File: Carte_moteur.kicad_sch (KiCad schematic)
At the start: 24 parts, among them J101 Conn_01x02_Socket, J102 Conn_01x02, J103 Conn_01x02, J104 Conn_01x05_Pin, J105 Conn_01x05_Pin, J106 Conn_01x05_Pin, J107 Conn_01x07, U101 LD1117S33TR_SOT223

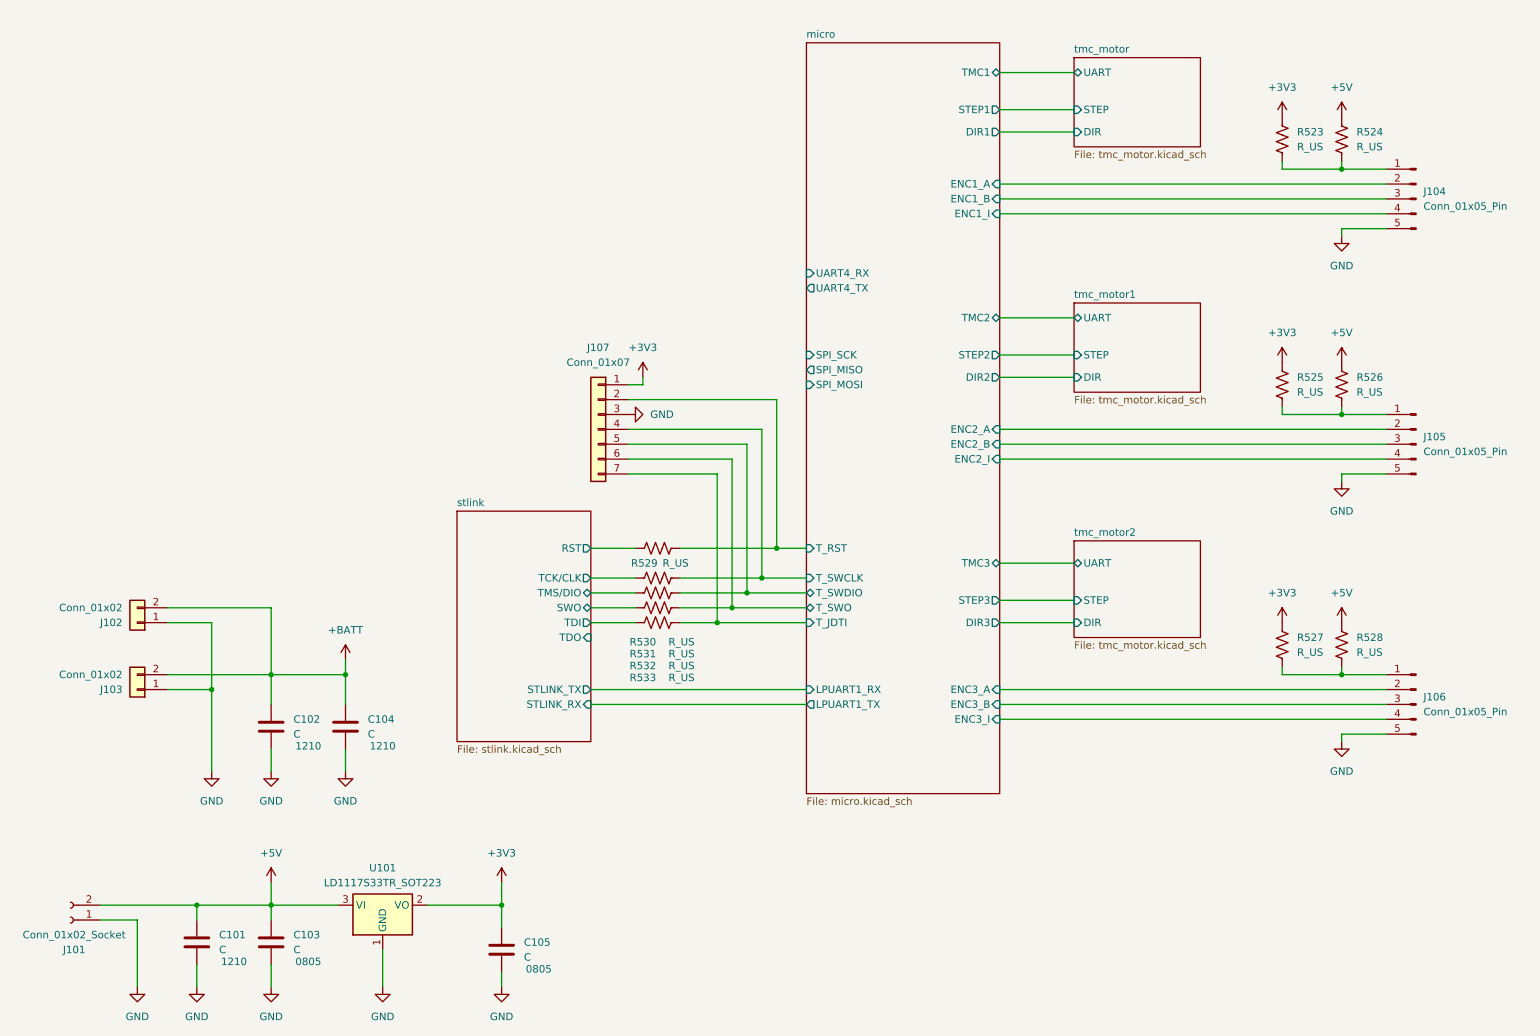
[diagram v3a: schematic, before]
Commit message: Add net class
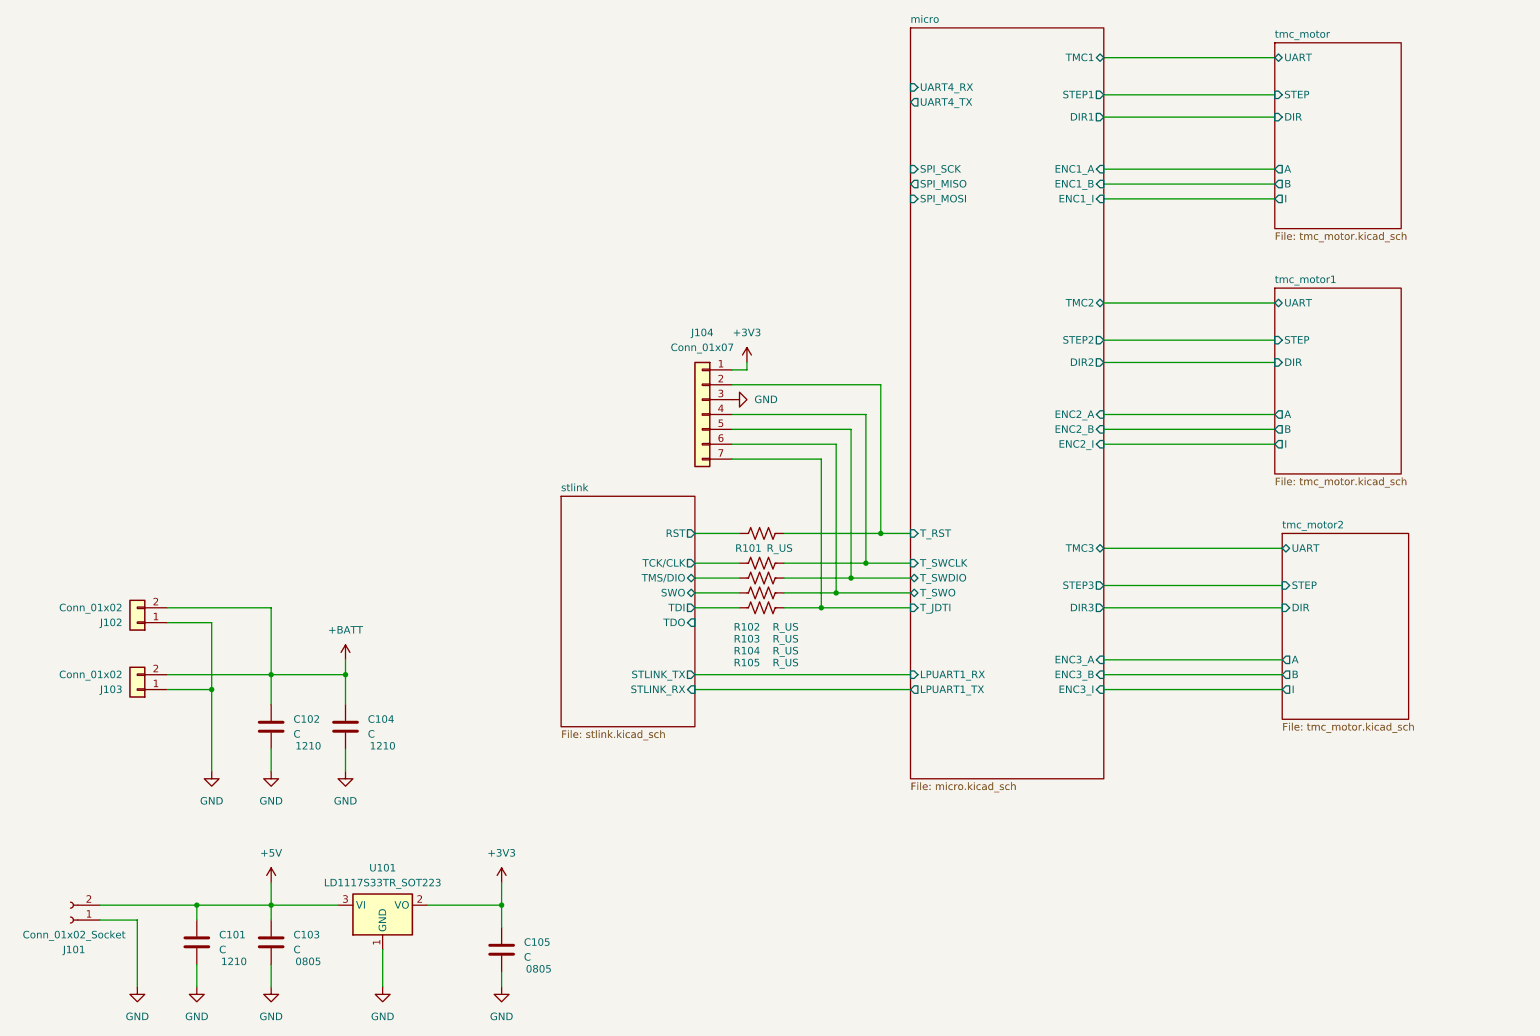
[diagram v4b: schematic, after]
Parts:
- removed J104, J105, J106: Conn_01x05_Pin, Connector_Molex:Molex_KK-254_AE-6410-05A_1x05_P2.54mm_Vertical, symbol Connector:Conn_01x05_Pin
- removed R523, R524, R525, R526, R527, R528: R_US, Resistor_SMD:R_0603_1608Metric_Pad0.98x0.95mm_HandSolder, symbol Device:R_US
- renumbered J107 to J104, R529 to R101, R530 to R102, R531 to R103, R532 to R104, R533 to R105
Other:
- sheet tmc_motor ports: added A, B, I; removed none
- sheet tmc_motor1 ports: added A, B, I; removed none
- sheet tmc_motor2 ports: added A, B, I; removed none
- moved on the sheet: J104, R101, R102, R103, R104, R105

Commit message: move encoder pull up resistor to tmc sheet
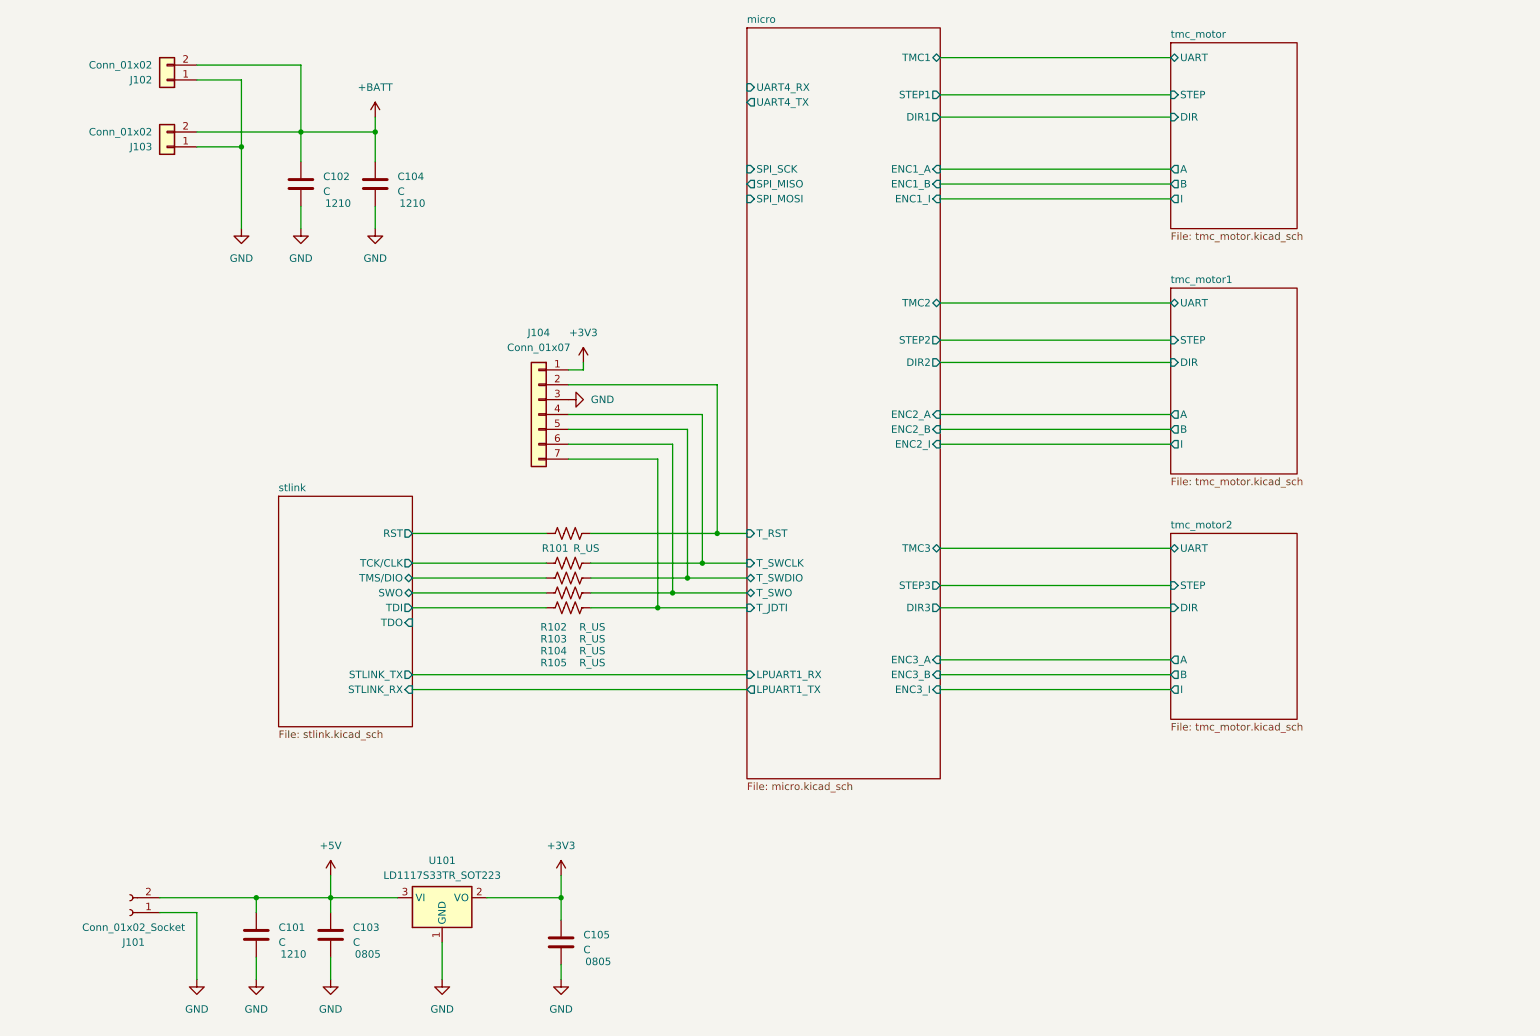
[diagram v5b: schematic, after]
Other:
- moved on the sheet: C101, C102, C103, C104, C105, J101, J102, J103, J104, R101, R102, R103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

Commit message: before trying new µC orientation
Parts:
- added J105: Conn_01x02_Socket, Connector_Molex:Molex_KK-396_A-41791-0002_1x02_P3.96mm_Vertical, symbol Connector:Conn_01x02_Socket
- added J106: Conn_01x07, Connector_Molex:Molex_KK-254_AE-6410-07A_1x07_P2.54mm_Vertical, symbol Connector_Generic:Conn_01x07
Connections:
- net +5V: now also J105.2 (Pin_2)
- net GND: now also J105.1 (Pin_1), J106.1 (Pin_1), J106.4 (Pin_4)
- net micro/SPI_MISO: now also J106.6 (Pin_6)
- net micro/SPI_MOSI: now also J106.7 (Pin_7)
- net micro/SPI_SCK: now also J106.5 (Pin_5)
- net micro/UART4_RX: now also J106.2 (Pin_2)
- net micro/UART4_TX: now also J106.3 (Pin_3)

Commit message: almost done
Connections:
- net micro/LPUART1_RX: now also J106.2 (Pin_2)
- net micro/LPUART1_TX: now also J106.3 (Pin_3)
- net micro/T_JDTI: now also J104.6 (Pin_6); no longer J104.7 (Pin_7)
- net micro/T_SWCLK: now also J104.5 (Pin_5); no longer J104.4 (Pin_4)
- net micro/T_SWDIO: now also J104.4 (Pin_4); no longer J104.5 (Pin_5)
- net micro/T_SWO: now also J104.7 (Pin_7); no longer J104.6 (Pin_6)
- net micro/UART4_RX: no longer J106.2 (Pin_2)
- net micro/UART4_TX: no longer J106.3 (Pin_3)
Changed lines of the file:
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@@
 	)
 	(junction
+		(at 124.46 118.11)
+		(diameter 0)
+		(color 0 0 0 0)
+	)
+	(junction
 		(at 45.72 172.72)
 		(diameter 0)
@@
 	)
 	(junction
-		(at 127 118.11)
+		(at 129.54 113.03)
 		(diameter 0)
 		(color 0 0 0 0)
 	)
 	(junction
-		(at 129.54 115.57)
+		(at 132.08 115.57)
 		(diameter 0)
 		(color 0 0 0 0)
 	)
 	(junction
-		(at 76.2 39.37)
+		(at 127 120.65)
 		(diameter 0)
 		(color 0 0 0 0)
 	)
 	(junction
-		(at 63.5 39.37)
+		(at 76.2 39.37)
 		(diameter 0)
 		(color 0 0 0 0)
 	)
 	(junction
-		(at 124.46 120.65)
+		(at 63.5 39.37)
 		(diameter 0)
 		(color 0 0 0 0)
@@
 		(color 0 0 0 0)
 	)
-	(junction
-		(at 132.08 113.03)
-		(diameter 0)
-		(color 0 0 0 0)
-	)
 	(wire
 		(pts
@@
 	(wire
 		(pts
-			(xy 129.54 90.17) (xy 129.54 115.57)
+			(xy 53.34 30.48) (xy 45.72 30.48)
 		)
 		(stroke
@@
 	(wire
 		(pts
-			(xy 53.34 30.48) (xy 45.72 30.48)
+			(xy 63.5 39.37) (xy 63.5 27.94)
 		)
 		(stroke
@@
 	(wire
 		(pts
-			(xy 63.5 39.37) (xy 63.5 27.94)
+			(xy 82.55 132.08) (xy 139.7 132.08)
 		)
 		(stroke
@@
 	(wire
 		(pts
-			(xy 113.03 113.03) (xy 132.08 113.03)
+			(xy 113.03 113.03) (xy 129.54 113.03)
+		)
+		(stroke
+			(width 0)
+			(type default)
+		)
+	)
+	(wire
+		(pts
+			(xy 124.46 118.11) (xy 139.7 118.11)
 		)
 		(stroke
@@
 	(wire
 		(pts
-			(xy 116.84 55.88) (xy 116.84 43.18)
+			(xy 109.22 38.1) (xy 139.7 38.1)
 		)
 		(stroke
@@
 	(wire
 		(pts
-			(xy 76.2 39.37) (xy 63.5 39.37)
+			(xy 116.84 55.88) (xy 116.84 43.18)
 		)
 		(stroke
@@
 	(wire
 		(pts
-			(xy 134.62 82.55) (xy 134.62 107.95)
+			(xy 127 92.71) (xy 127 120.65)
 		)
 		(stroke
@@
 	(wire
 		(pts
-			(xy 109.22 38.1) (xy 139.7 38.1)
+			(xy 76.2 39.37) (xy 63.5 39.37)
 		)
 		(stroke
@@
 	(wire
 		(pts
-			(xy 76.2 39.37) (xy 76.2 44.45)
+			(xy 134.62 82.55) (xy 134.62 107.95)
 		)
 		(stroke
@@
 	(wire
 		(pts
-			(xy 132.08 113.03) (xy 139.7 113.03)
+			(xy 76.2 39.37) (xy 76.2 44.45)
 		)
 		(stroke
@@
 	(wire
 		(pts
-			(xy 109.22 35.56) (xy 116.84 35.56)
+			(xy 132.08 115.57) (xy 139.7 115.57)
 		)
 		(stroke
@@
 	(wire
 		(pts
-			(xy 113.03 118.11) (xy 127 118.11)
+			(xy 109.22 35.56) (xy 116.84 35.56)
 		)
 		(stroke
@@
 	(wire
 		(pts
-			(xy 124.46 95.25) (xy 124.46 120.65)
-		)
-		(stroke
-			(width 0)
-			(type default)
-		)
-	)
-	(wire
-		(pts
 			(xy 172.72 78.74) (xy 212.09 78.74)
 		)
@@
 	(wire
 		(pts
-			(xy 172.72 48.26) (xy 212.09 48.26)
+			(xy 124.46 95.25) (xy 124.46 118.11)
 		)
 		(stroke
@@
 	(wire
 		(pts
-			(xy 109.22 92.71) (xy 127 92.71)
+			(xy 172.72 48.26) (xy 212.09 48.26)
 		)
 		(stroke
@@
 	(wire
 		(pts
-			(xy 82.55 115.57) (xy 105.41 115.57)
+			(xy 109.22 92.71) (xy 127 92.71)
 		)
 		(stroke
@@
 	(wire
 		(pts
-			(xy 172.72 33.02) (xy 212.09 33.02)
+			(xy 82.55 115.57) (xy 105.41 115.57)
 		)
 		(stroke
@@
 	(wire
 		(pts
-			(xy 82.55 134.62) (xy 139.7 134.62)
+			(xy 172.72 33.02) (xy 212.09 33.02)
 		)
 		(stroke
@@
 	(wire
 		(pts
-			(xy 113.03 115.57) (xy 129.54 115.57)
+			(xy 113.03 115.57) (xy 132.08 115.57)
 		)
 		(stroke
@@
 	(wire
 		(pts
-			(xy 113.03 120.65) (xy 124.46 120.65)
+			(xy 113.03 118.11) (xy 124.46 118.11)
 		)
 		(stroke
@@
 	(wire
 		(pts
-			(xy 127 118.11) (xy 139.7 118.11)
+			(xy 109.22 82.55) (xy 134.62 82.55)
 		)
 		(stroke
@@
 	(wire
 		(pts
-			(xy 109.22 82.55) (xy 134.62 82.55)
+			(xy 95.25 170.18) (xy 107.95 170.18)
 		)
 		(stroke
@@
 	(wire
 		(pts
-			(xy 95.25 170.18) (xy 107.95 170.18)
+			(xy 113.03 107.95) (xy 134.62 107.95)
 		)
 		(stroke
@@
 	(wire
 		(pts
-			(xy 113.03 107.95) (xy 134.62 107.95)
+			(xy 116.84 43.18) (xy 109.22 43.18)
 		)
 		(stroke
@@
 	(wire
 		(pts
-			(xy 127 92.71) (xy 127 118.11)
+			(xy 129.54 90.17) (xy 129.54 113.03)
 		)
 		(stroke
@@
 	(wire
 		(pts
-			(xy 116.84 43.18) (xy 109.22 43.18)
+			(xy 129.54 113.03) (xy 139.7 113.03)
 		)
 		(stroke
@@
 	(wire
 		(pts
-			(xy 39.37 158.75) (xy 45.72 158.75)
+			(xy 109.22 40.64) (xy 139.7 40.64)
 		)
 		(stroke
@@
 	(wire
 		(pts
-			(xy 68.58 166.37) (xy 68.58 170.18)
+			(xy 39.37 158.75) (xy 45.72 158.75)
 		)
 		(stroke
@@
 	(wire
 		(pts
-			(xy 172.72 116.84) (xy 212.09 116.84)
+			(xy 68.58 166.37) (xy 68.58 170.18)
 		)
 		(stroke
@@
 	(wire
 		(pts
-			(xy 55.88 170.18) (xy 55.88 172.72)
+			(xy 172.72 116.84) (xy 212.09 116.84)
 		)
 		(stroke
@@
 	(wire
 		(pts
-			(xy 172.72 134.62) (xy 212.09 134.62)
+			(xy 55.88 170.18) (xy 55.88 172.72)
 		)
 		(stroke
@@
 	(wire
 		(pts
-			(xy 109.22 90.17) (xy 129.54 90.17)
+			(xy 172.72 134.62) (xy 212.09 134.62)
 		)
 		(stroke
@@
 	(wire
 		(pts
-			(xy 82.55 132.08) (xy 139.7 132.08)
+			(xy 109.22 90.17) (xy 129.54 90.17)
 		)
 		(stroke
@@
 	(wire
 		(pts
-			(xy 172.72 36.83) (xy 212.09 36.83)
+			(xy 132.08 87.63) (xy 132.08 115.57)
 		)
 		(stroke
@@
 	(wire
 		(pts
-			(xy 109.22 40.64) (xy 139.7 40.64)
+			(xy 172.72 36.83) (xy 212.09 36.83)
 		)
 		(stroke
@@
 	(wire
 		(pts
-			(xy 129.54 115.57) (xy 139.7 115.57)
-		)
-		(stroke
-			(width 0)
-			(type default)
-		)
-	)
-	(wire
-		(pts
-			(xy 132.08 87.63) (xy 132.08 113.03)
+			(xy 45.72 27.94) (xy 63.5 27.94)
 		)
 		(stroke
@@
 	(wire
 		(pts
-			(xy 45.72 27.94) (xy 63.5 27.94)
+			(xy 127 120.65) (xy 139.7 120.65)
 		)
 		(stroke
@@
 	(wire
 		(pts
-			(xy 124.46 120.65) (xy 139.7 120.65)
+			(xy 113.03 120.65) (xy 127 120.65)
 		)
 		(stroke
@@
 		)
 	)
+	(wire
+		(pts
+			(xy 82.55 134.62) (xy 139.7 134.62)
+		)
+		(stroke
+			(width 0)
+			(type default)
+		)
+	)
 	(netclass_flag ""
 		(length 2.54)
@@
 		)
 		(pin "UART4_RX" input
-			(at 139.7 38.1 180)
+			(at 139.7 132.08 180)
 			(effects
 				(font
@@
 		)
 		(pin "UART4_TX" output
-			(at 139.7 40.64 180)
+			(at 139.7 134.62 180)
 			(effects
 				(font
@@
 		)
 		(pin "LPUART1_RX" input
-			(at 139.7 132.08 180)
+			(at 139.7 38.1 180)
 			(effects
 				(font
@@
 		)
 		(pin "LPUART1_TX" output
-			(at 139.7 134.62 180)
+			(at 139.7 40.64 180)
 			(effects
 				(font

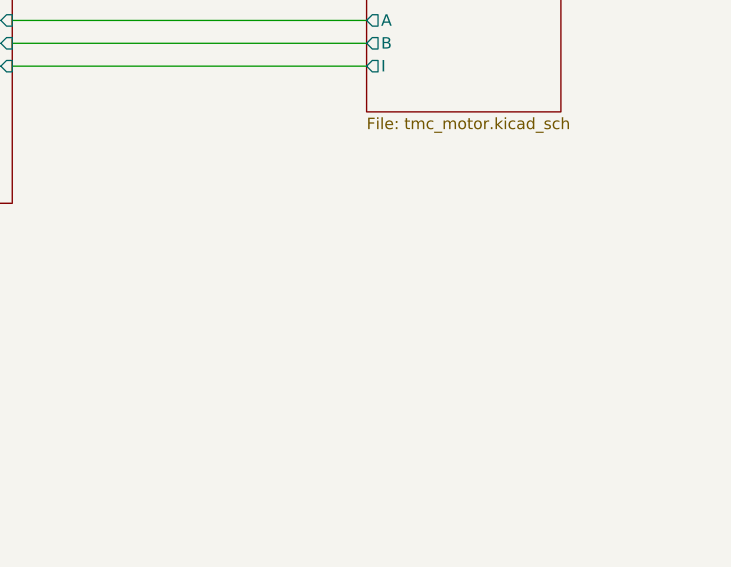
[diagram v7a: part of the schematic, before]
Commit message: silk and holes ok
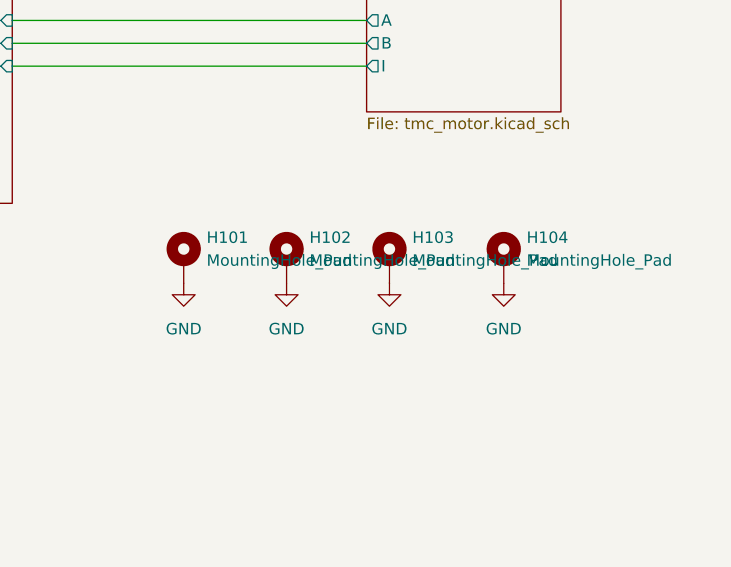
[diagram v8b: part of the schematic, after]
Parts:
- added H101, H102, H103, H104: MountingHole_Pad, MountingHole:MountingHole_3.2mm_M3_DIN965_Pad, symbol Mechanical:MountingHole_Pad
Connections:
- net GND: now also H101.1, H102.1, H103.1, H104.1
